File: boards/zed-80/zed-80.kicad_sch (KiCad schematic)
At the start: 0 parts

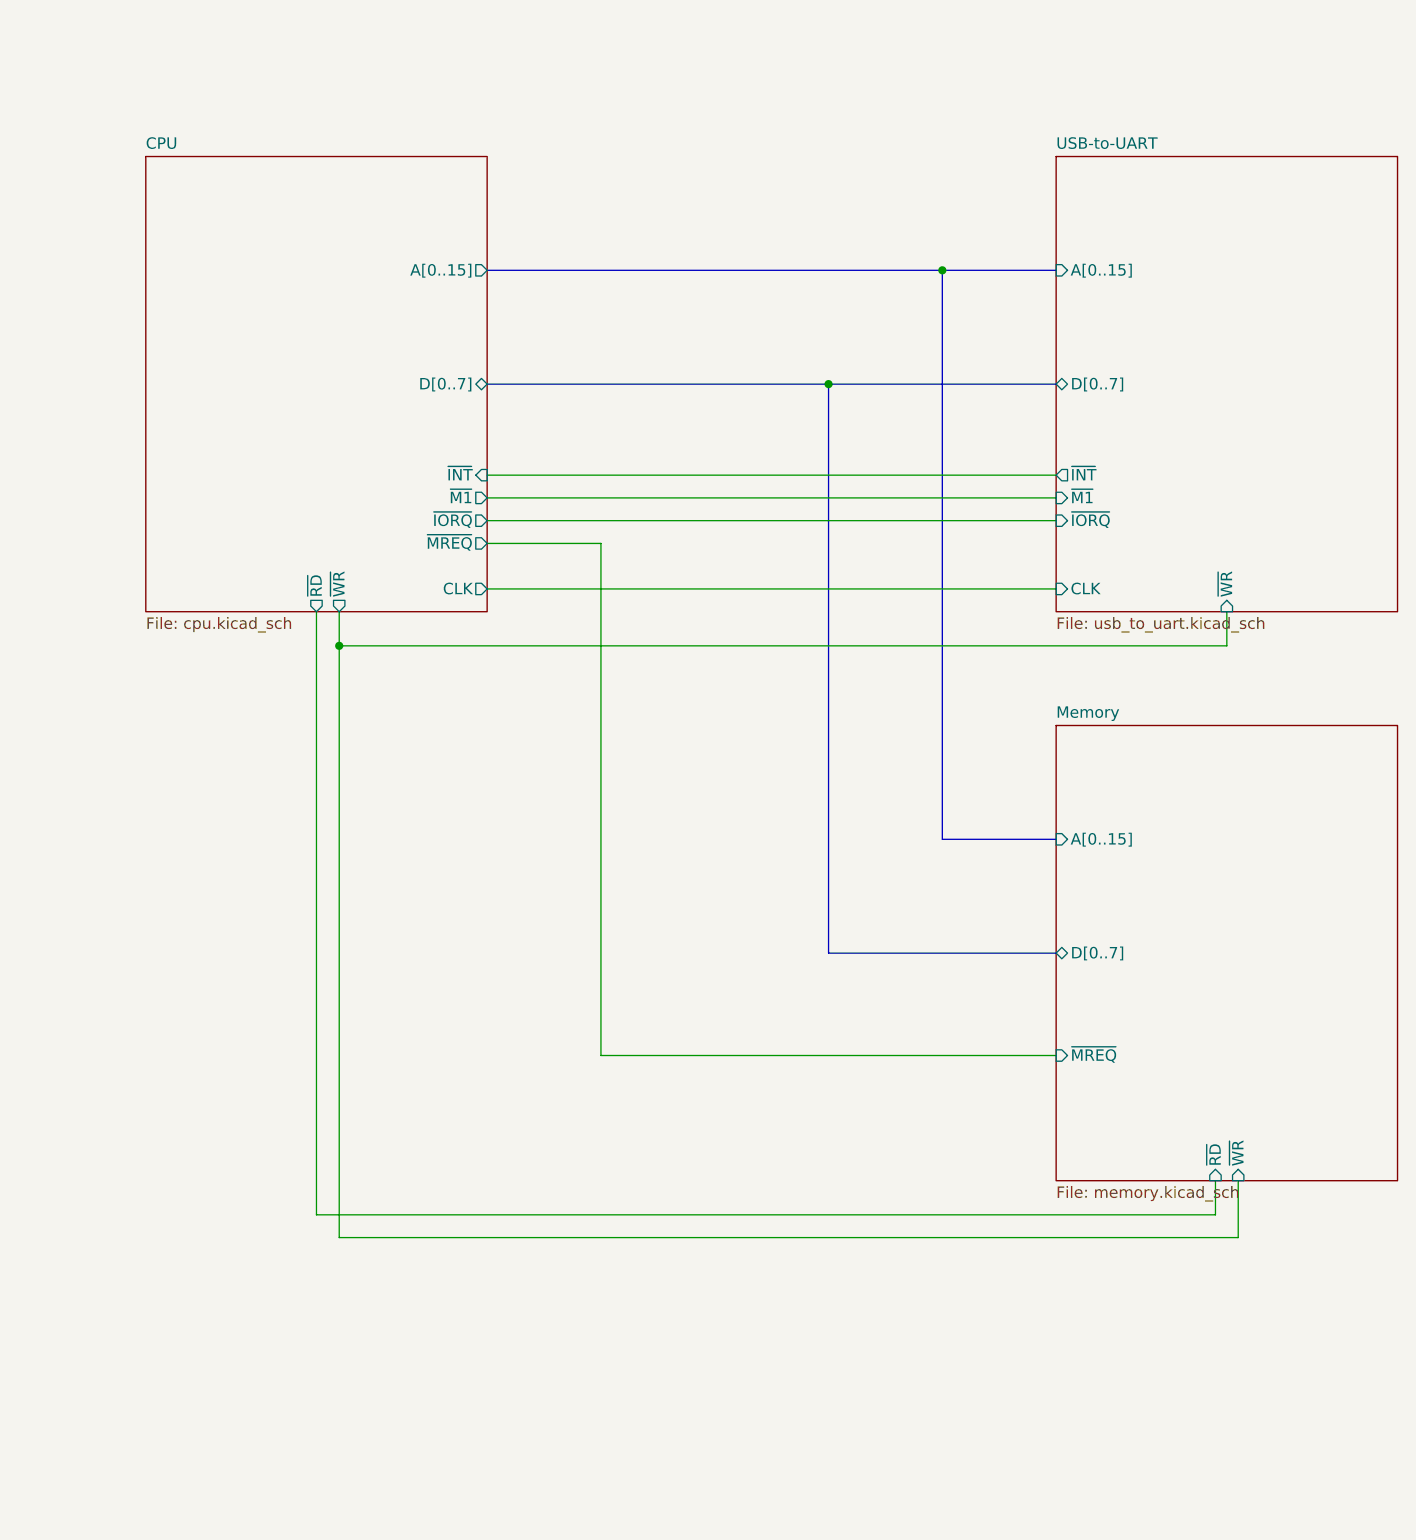
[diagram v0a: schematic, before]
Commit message: Polished schematics and basic PCB setup
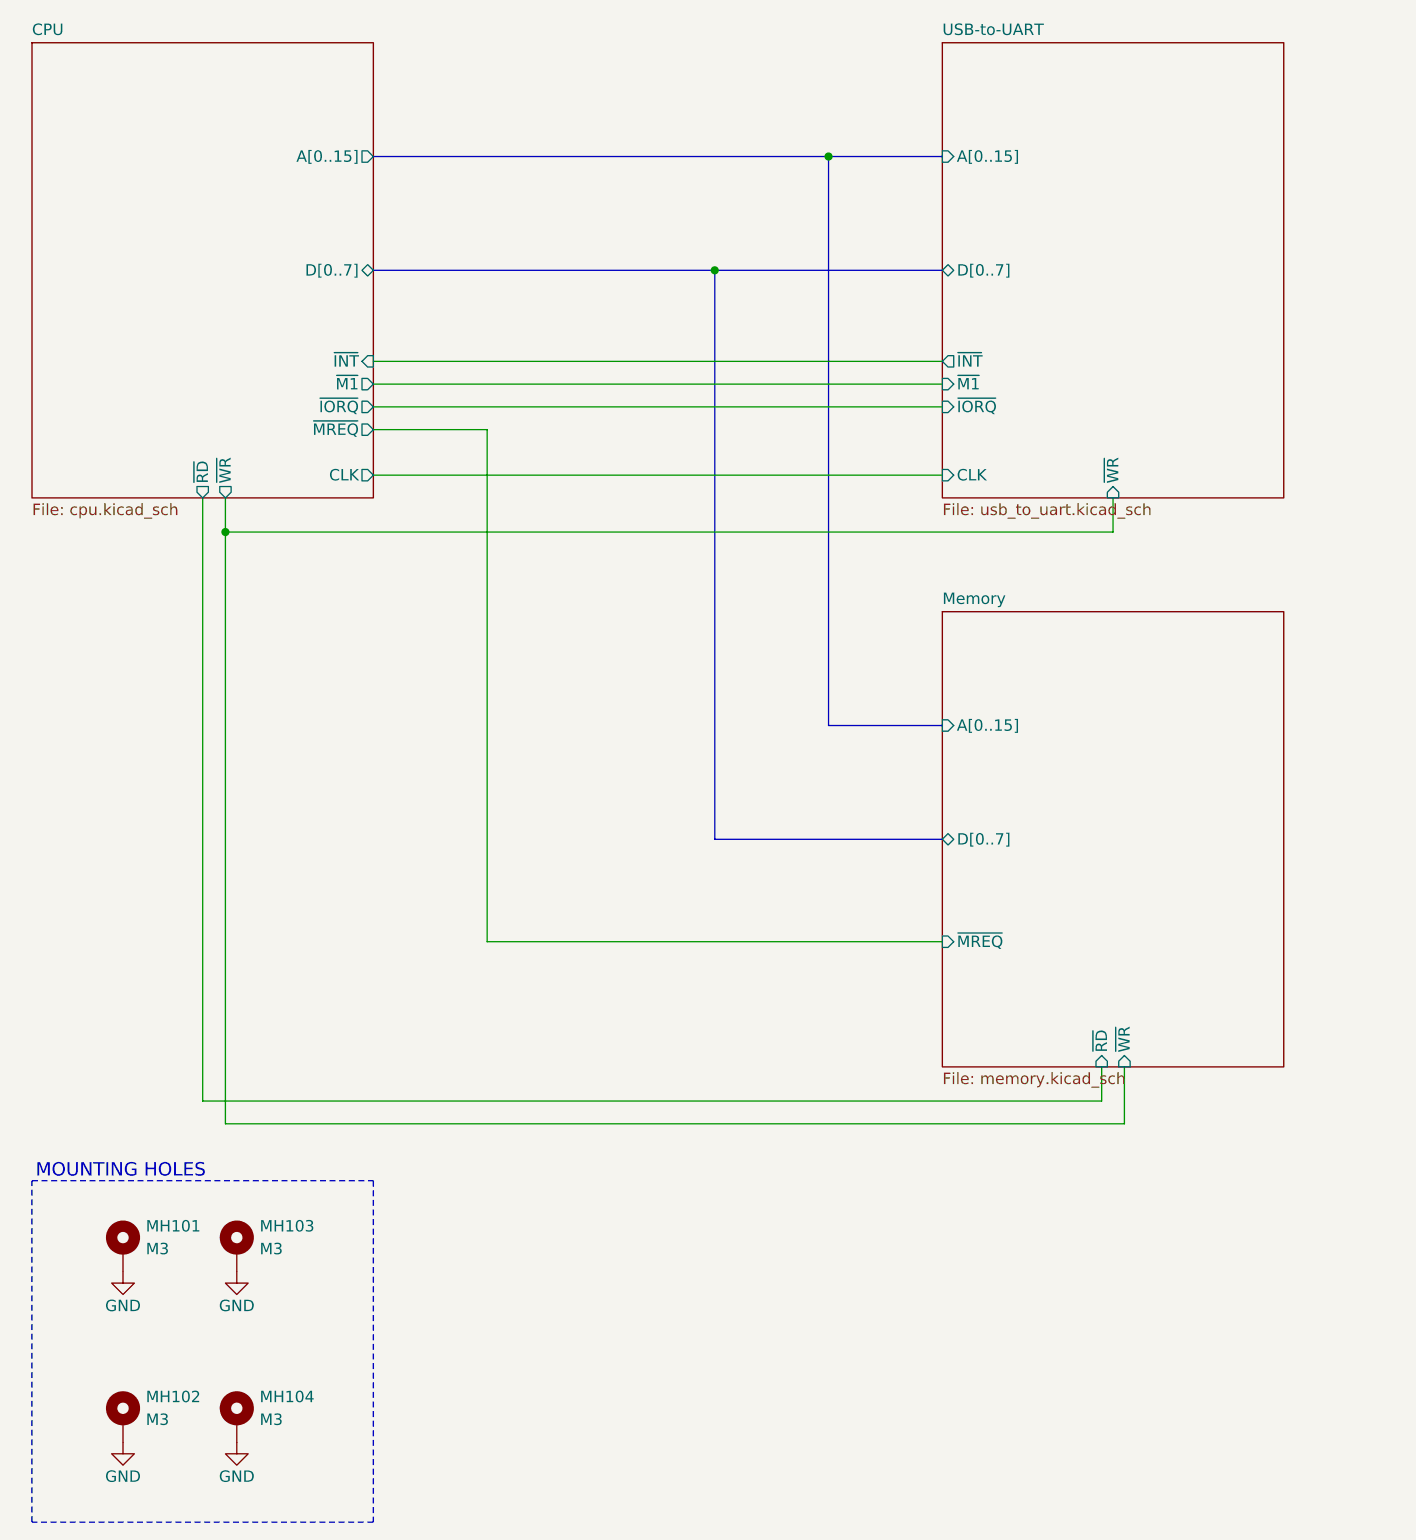
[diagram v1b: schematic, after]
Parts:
- added MH101, MH102, MH103, MH104: M3, MountingHole:MountingHole_3.2mm_M3_Pad_Via, symbol Mechanical:MountingHole_Pad
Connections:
- new net GND: MH101.1, MH102.1, MH103.1, MH104.1
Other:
- note added: "MOUNTING HOLES"
- company: (none) -> Dragos Bajanica
- title: (none) -> zed-80
